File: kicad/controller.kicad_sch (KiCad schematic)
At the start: 16 parts, among them J9 SWD, SW6 RESET, U6 Pico, U7 LM4040CIM3-3.0/NOPB

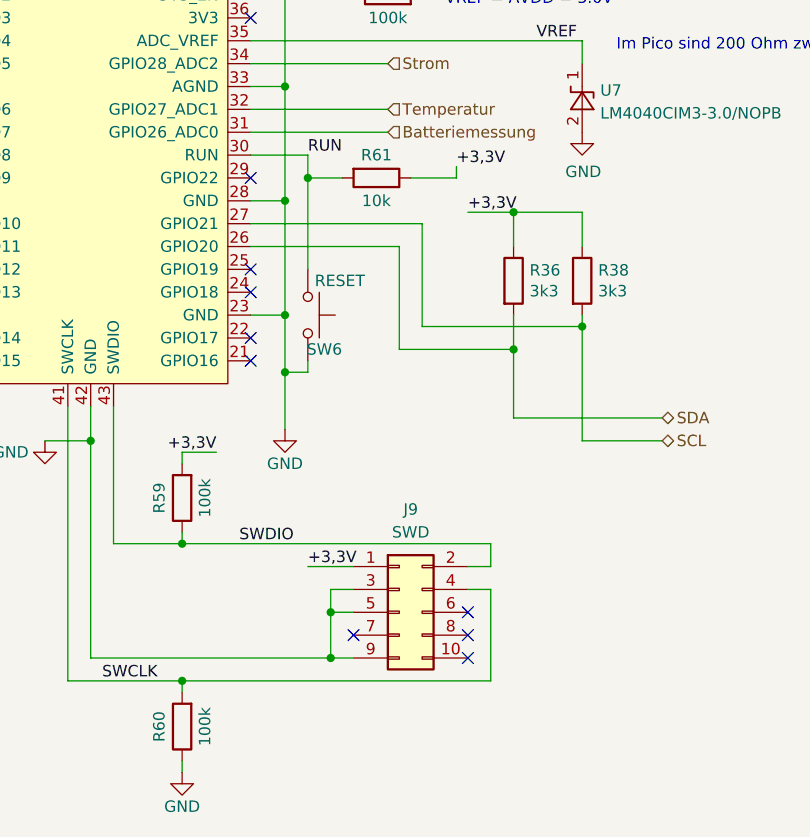
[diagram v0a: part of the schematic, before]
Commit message: created bom for order lcsc
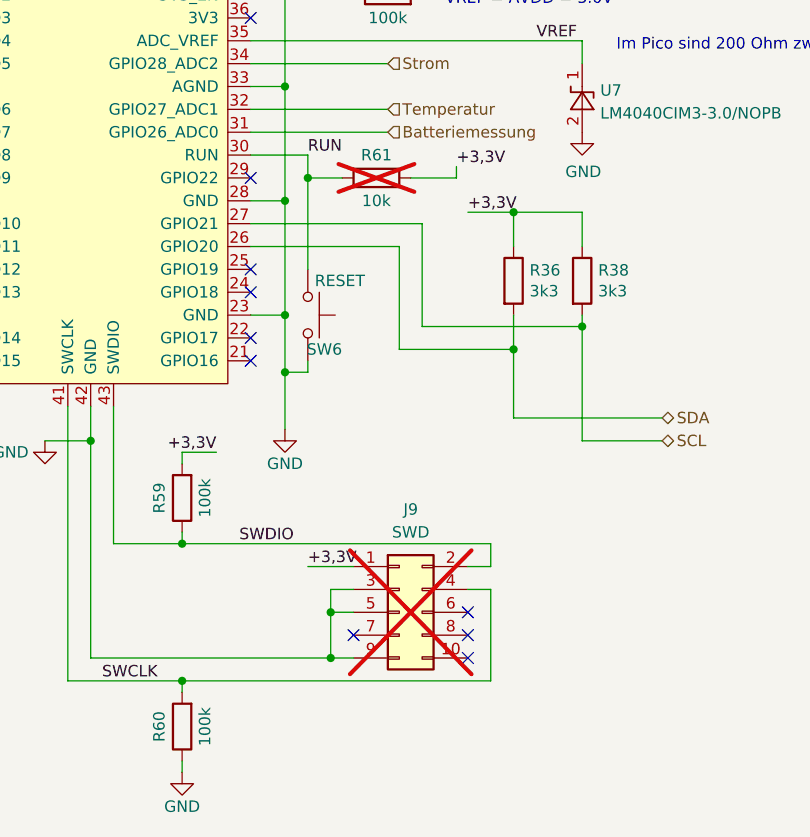
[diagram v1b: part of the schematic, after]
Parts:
- J9, R61: now not fitted; now left out of the parts list
